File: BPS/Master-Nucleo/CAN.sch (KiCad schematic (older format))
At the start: 23 parts, among them J5 CAN_Out, U4 CDSOT23-T24CAN, U5 ADM3055E

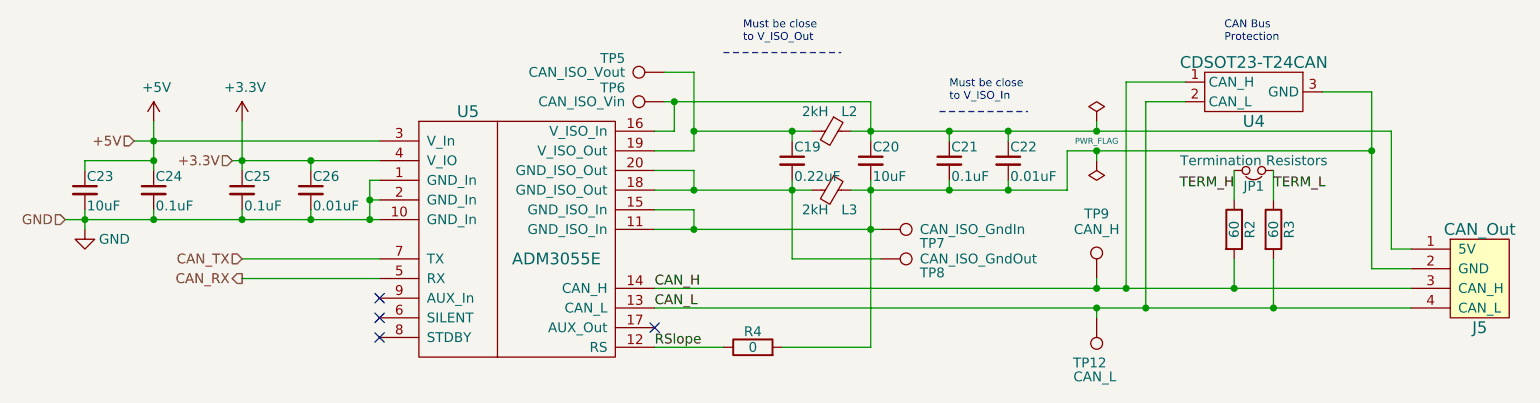
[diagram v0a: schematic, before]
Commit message: Adds Nucleo version of master board.
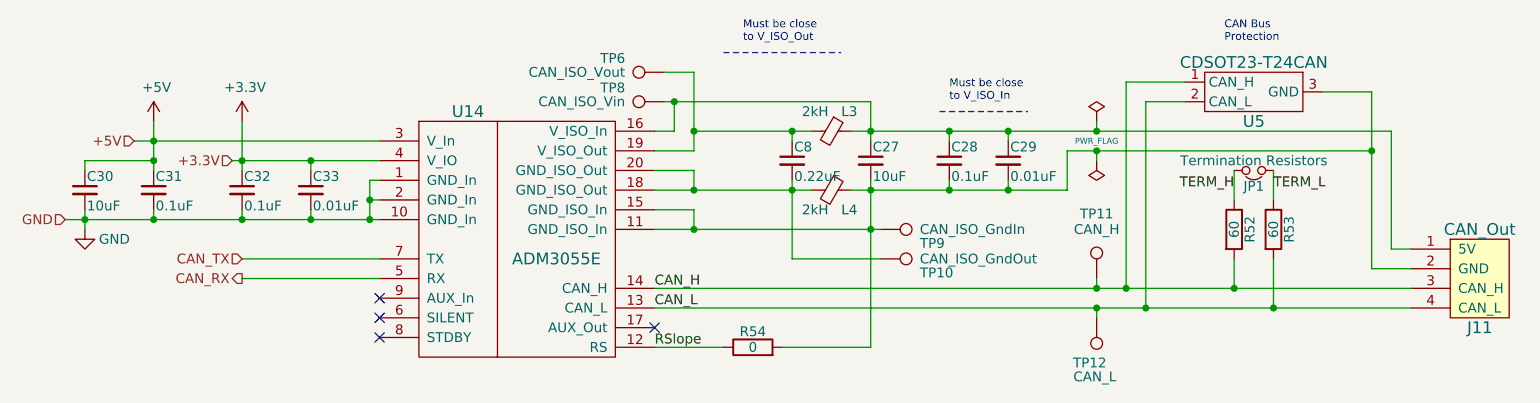
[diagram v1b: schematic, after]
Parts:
- renumbered C20 to C27, C21 to C28, C22 to C29, C23 to C30, C24 to C31, C25 to C32, C26 to C33, C19 to C8, J5 to J11, L2 to L3, L3 to L4, R2 to R52, R3 to R53, R4 to R54, TP8 to TP10, TP9 to TP11, TP5 to TP6, TP6 to TP8, TP7 to TP9, U5 to U14, U4 to U5
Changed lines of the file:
@@
 EESchema Schematic File Version 4
-LIBS:BPSMaster-cache
 EELAYER 29 0
 EELAYER END
 $Descr A4 11693 8268
 encoding utf-8
-Sheet 3 7
+Sheet 7 7
 Title ""
 Date ""
@@
 $EndDescr
 $Comp
-L utsvt-connectors:CANConnector J5
+L utsvt-connectors:CANConnector J11
 U 1 1 5C2B42F3
 P 9250 3800
-F 0 "J5" H 9250 3550 60  0000 C CNN
+F 0 "J11" H 9250 3550 60  0000 C CNN
 F 1 "CAN_Out" H 9250 4050 60  0000 C CNN
 F 2 "UTSVT_Connectors:Molex_MicroFit3.0_1x4xP3.00mm_PolarizingPeg_Vertical" H 9400 4100 60  0001 C CNN
@@
 $EndComp
 $Comp
-L Device:R R3
+L Device:R R53
 U 1 1 5C2B42FA
 P 8200 3550
-F 0 "R3" V 8280 3550 50  0000 C CNN
+F 0 "R53" V 8280 3550 50  0000 C CNN
 F 1 "60" V 8200 3550 50  0000 C CNN
 F 2 "Resistor_SMD:R_0805_2012Metric" V 8130 3550 50  0001 C CNN
@@
 $EndComp
 $Comp
-L Device:R R2
+L Device:R R52
 U 1 1 5C2B4301
 P 8000 3550
-F 0 "R2" V 8080 3550 50  0000 C CNN
+F 0 "R52" V 8080 3550 50  0000 C CNN
 F 1 "60" V 8000 3550 50  0000 C CNN
 F 2 "Resistor_SMD:R_0805_2012Metric" V 7930 3550 50  0001 C CNN
@@
 $EndComp
 $Comp
-L Device:C_Small C23
+L Device:C_Small C30
 U 1 1 5C2B4310
 P 2150 3350
-F 0 "C23" H 2160 3420 50  0000 L CNN
+F 0 "C30" H 2160 3420 50  0000 L CNN
 F 1 "10uF" H 2160 3270 50  0000 L CNN
 F 2 "Capacitor_SMD:C_0805_2012Metric" H 2150 3350 50  0001 C CNN
@@
 $EndComp
 $Comp
-L Device:C_Small C24
+L Device:C_Small C31
 U 1 1 5C2B4317
 P 2500 3350
-F 0 "C24" H 2510 3420 50  0000 L CNN
+F 0 "C31" H 2510 3420 50  0000 L CNN
 F 1 "0.1uF" H 2510 3270 50  0000 L CNN
 F 2 "Capacitor_SMD:C_0805_2012Metric" H 2500 3350 50  0001 C CNN
@@
 $EndComp
 $Comp
-L Device:C_Small C25
+L Device:C_Small C32
 U 1 1 5C2B431E
 P 2950 3350
-F 0 "C25" H 2960 3420 50  0000 L CNN
+F 0 "C32" H 2960 3420 50  0000 L CNN
 F 1 "0.1uF" H 2960 3270 50  0000 L CNN
 F 2 "Capacitor_SMD:C_0805_2012Metric" H 2950 3350 50  0001 C CNN
@@
 $EndComp
 $Comp
-L Device:C_Small C26
+L Device:C_Small C33
 U 1 1 5C2B4325
 P 3300 3350
-F 0 "C26" H 3310 3420 50  0000 L CNN
+F 0 "C33" H 3310 3420 50  0000 L CNN
 F 1 "0.01uF" H 3310 3270 50  0000 L CNN
 F 2 "Capacitor_SMD:C_0805_2012Metric" H 3300 3350 50  0001 C CNN
@@
 $EndComp
 $Comp
-L Device:C_Small C20
+L Device:C_Small C27
 U 1 1 5C2B432E
 P 6150 3200
-F 0 "C20" H 6160 3270 50  0000 L CNN
+F 0 "C27" H 6160 3270 50  0000 L CNN
 F 1 "10uF" H 6160 3120 50  0000 L CNN
 F 2 "Capacitor_SMD:C_0805_2012Metric" H 6150 3200 50  0001 C CNN
@@
 $EndComp
 $Comp
-L Device:C_Small C19
+L Device:C_Small C8
 U 1 1 5C2B4335
 P 5750 3200
-F 0 "C19" H 5760 3270 50  0000 L CNN
+F 0 "C8" H 5760 3270 50  0000 L CNN
 F 1 "0.22uF" H 5760 3120 50  0000 L CNN
 F 2 "Capacitor_SMD:C_0805_2012Metric" H 5750 3200 50  0001 C CNN
@@
 $EndComp
 $Comp
-L Device:Ferrite_Bead_Small L2
+L Device:Ferrite_Bead_Small L3
 U 1 1 5C2B433C
 P 5950 3050
-F 0 "L2" V 5850 3100 50  0000 L CNN
+F 0 "L3" V 5850 3100 50  0000 L CNN
 F 1 "2kH" V 5850 2900 50  0000 L CNN
 F 2 "Inductor_SMD:L_0805_2012Metric" V 5880 3050 50  0001 C CNN
@@
 $EndComp
 $Comp
-L Device:Ferrite_Bead_Small L3
+L Device:Ferrite_Bead_Small L4
 U 1 1 5C2B4343
 P 5950 3350
-F 0 "L3" V 6050 3400 50  0000 L CNN
+F 0 "L4" V 6050 3400 50  0000 L CNN
 F 1 "2kH" V 6050 3200 50  0000 L CNN
 F 2 "Inductor_SMD:L_0805_2012Metric" V 5880 3350 50  0001 C CNN
@@
 $EndComp
 $Comp
-L Device:C_Small C21
+L Device:C_Small C28
 U 1 1 5C2B434A
 P 6550 3200
-F 0 "C21" H 6560 3270 50  0000 L CNN
+F 0 "C28" H 6560 3270 50  0000 L CNN
 F 1 "0.1uF" H 6560 3120 50  0000 L CNN
 F 2 "Capacitor_SMD:C_0805_2012Metric" H 6550 3200 50  0001 C CNN
@@
 $EndComp
 $Comp
-L Device:C_Small C22
+L Device:C_Small C29
 U 1 1 5C2B4351
 P 6850 3200
-F 0 "C22" H 6860 3270 50  0000 L CNN
+F 0 "C29" H 6860 3270 50  0000 L CNN
 F 1 "0.01uF" H 6860 3120 50  0000 L CNN
 F 2 "Capacitor_SMD:C_0805_2012Metric" H 6850 3200 50  0001 C CNN
@@
 $EndComp
 $Comp
-L utsvt-chips:ADM3055E U5
+L utsvt-chips:ADM3055E U14
 U 1 1 5C2B4359
 P 4350 3600
-F 0 "U5" H 4100 4250 60  0000 C CNN
+F 0 "U14" H 4100 4250 60  0000 C CNN
 F 1 "ADM3055E" H 4550 3500 60  0000 C CNN
 F 2 "UTSVT_ICs:SOIC-20W_7.5x15.4mm_Pitch1.27mm" H 4350 3700 60  0001 C CNN
@@
 Must be close\nto V_ISO_In
 $Comp
-L Connector:TestPoint TP6
+L Connector:TestPoint TP8
 U 1 1 5C2B4371
 P 5100 2900
-F 0 "TP6" V 5200 3100 50  0000 L BNN
+F 0 "TP8" V 5200 3100 50  0000 L BNN
 F 1 "CAN_ISO_Vin" V 5100 3100 50  0000 L CNN
 F 2 "TestPoint:TestPoint_Keystone_5005-5009_Compact" H 5100 2900 50  0001 C CNN
@@
 $EndComp
 $Comp
-L Connector:TestPoint TP8
+L Connector:TestPoint TP10
 U 1 1 5C2B4378
 P 6200 3700
-F 0 "TP8" V 6300 3900 50  0000 L BNN
+F 0 "TP10" V 6300 3900 50  0000 L BNN
 F 1 "CAN_ISO_GndOut" V 6200 3900 50  0000 L CNN
 F 2 "TestPoint:TestPoint_Keystone_5005-5009_Compact" H 6200 3700 50  0001 C CNN
@@
 $EndComp
 $Comp
-L Connector:TestPoint TP7
+L Connector:TestPoint TP9
 U 1 1 5C2B437F
 P 6200 3550
-F 0 "TP7" V 6300 3750 50  0000 L BNN
+F 0 "TP9" V 6300 3750 50  0000 L BNN
 F 1 "CAN_ISO_GndIn" V 6200 3750 50  0000 L CNN
 F 2 "TestPoint:TestPoint_Keystone_5005-5009_Compact" H 6200 3550 50  0001 C CNN
@@
 $EndComp
 $Comp
-L Connector:TestPoint TP5
+L Connector:TestPoint TP6
 U 1 1 5C2B4386
 P 5100 2750
-F 0 "TP5" V 5200 2950 50  0000 L BNN
+F 0 "TP6" V 5200 2950 50  0000 L BNN
 F 1 "CAN_ISO_Vout" V 5100 2950 50  0000 L CNN
 F 2 "TestPoint:TestPoint_Keystone_5005-5009_Compact" H 5100 2750 50  0001 C CNN
@@
 NoConn ~ 3650 4100
 $Comp
-L power:PWR_FLAG #FLG03
+L power:PWR_FLAG #FLG0104
 U 1 1 5C2B4394
 P 7300 3000
-F 0 "#FLG03" H 7300 3075 50  0001 C CNN
+F 0 "#FLG0104" H 7300 3075 50  0001 C CNN
 F 1 "PWR_FLAG" H 7300 2900 30  0000 C CNN
 F 2 "" H 7300 3000 50  0001 C CNN
@@
 $EndComp
 $Comp
-L power:PWR_FLAG #FLG04
+L power:PWR_FLAG #FLG0105
 U 1 1 5C2B439A
 P 7300 3200
-F 0 "#FLG04" H 7300 3275 50  0001 C CNN
+F 0 "#FLG0105" H 7300 3275 50  0001 C CNN
 F 1 "PWR_FLAG" H 7200 3150 50  0001 L CNN
 F 2 "" H 7300 3200 50  0001 C CNN
@@
 $EndComp
 $Comp
-L utsvt-chips:CDSOT23-T24CAN U4
+L utsvt-chips:CDSOT23-T24CAN U5
 U 1 1 5C2B43A0
 P 8100 2850
-F 0 "U4" H 8100 2700 60  0000 C CNN
+F 0 "U5" H 8100 2700 60  0000 C CNN
 F 1 "CDSOT23-T24CAN" H 8100 3000 60  0000 C CNN
 F 2 "Package_TO_SOT_SMD:SOT-23W" H 8100 2850 60  0001 C CNN
@@
 CAN Bus\nProtection
 $Comp
-L Connector:TestPoint TP9
+L Connector:TestPoint TP11
 U 1 1 5C2B43B6
 P 7300 3800
-F 0 "TP9" H 7300 4100 50  0000 C BNN
+F 0 "TP11" H 7300 4100 50  0000 C BNN
 F 1 "CAN_H" H 7300 4050 50  0000 C CNN
 F 2 "TestPoint:TestPoint_Keystone_5005-5009_Compact" H 7300 3800 50  0001 C CNN
@@
 $EndComp
 $Comp
-L Device:R R4
+L Device:R R54
 U 1 1 5C2B43C4
 P 5550 4150
-F 0 "R4" V 5630 4150 50  0000 C CNN
+F 0 "R54" V 5630 4150 50  0000 C CNN
 F 1 "0" V 5550 4150 50  0000 C CNN
 F 2 "Resistor_SMD:R_0805_2012Metric" V 5480 4150 50  0001 C CNN
@@
 	6150 3550 6200 3550
 $Comp
-L power:GND #PWR042
+L power:GND #PWR0194
 U 1 1 5C28BDDE
 P 2150 3550
-F 0 "#PWR042" H 2150 3300 50  0001 C CNN
+F 0 "#PWR0194" H 2150 3300 50  0001 C CNN
 F 1 "GND" H 2300 3500 50  0000 C CNN
 F 2 "" H 2150 3550 50  0001 C CNN
@@
 	2500 3000 2500 3100
 $Comp
-L power:+3.3V #PWR0133
+L power:+3.3V #PWR0195
 U 1 1 5C4ABE05
 P 2950 3000
-F 0 "#PWR0133" H 2950 2850 50  0001 C CNN
+F 0 "#PWR0195" H 2950 2850 50  0001 C CNN
 F 1 "+3.3V" H 2965 3173 50  0000 C CNN
 F 2 "" H 2950 3000 50  0001 C CNN
@@
 	2950 3000 2950 3200
 $Comp
-L power:+5V #PWR0132
+L power:+5V #PWR0196
 U 1 1 5C4C2AB0
 P 2500 3000
-F 0 "#PWR0132" H 2500 2850 50  0001 C CNN
+F 0 "#PWR0196" H 2500 2850 50  0001 C CNN
 F 1 "+5V" H 2515 3173 50  0000 C CNN
 F 2 "" H 2500 3000 50  0001 C CNN
